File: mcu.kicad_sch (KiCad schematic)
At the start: 1 part, among them U1 MIMXRT1052CVJ5B

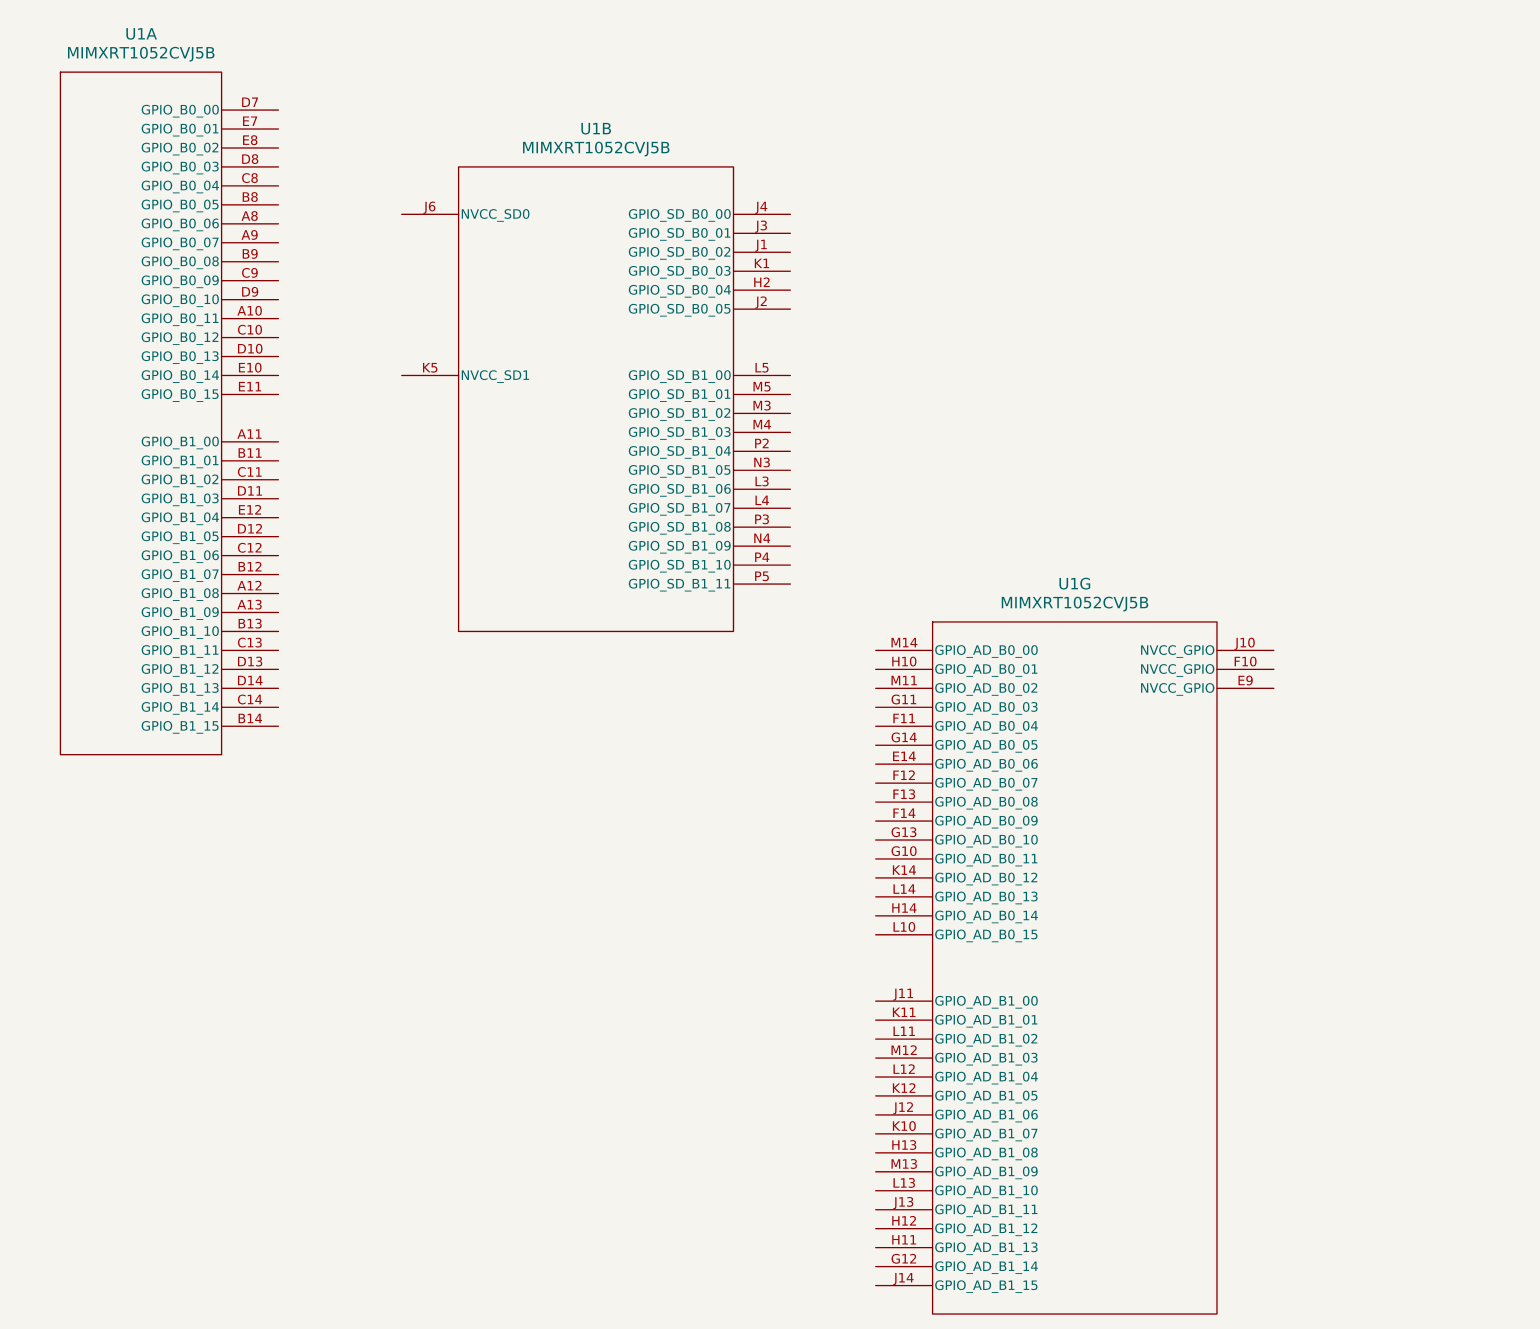
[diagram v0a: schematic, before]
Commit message: assign pin functions and started spe
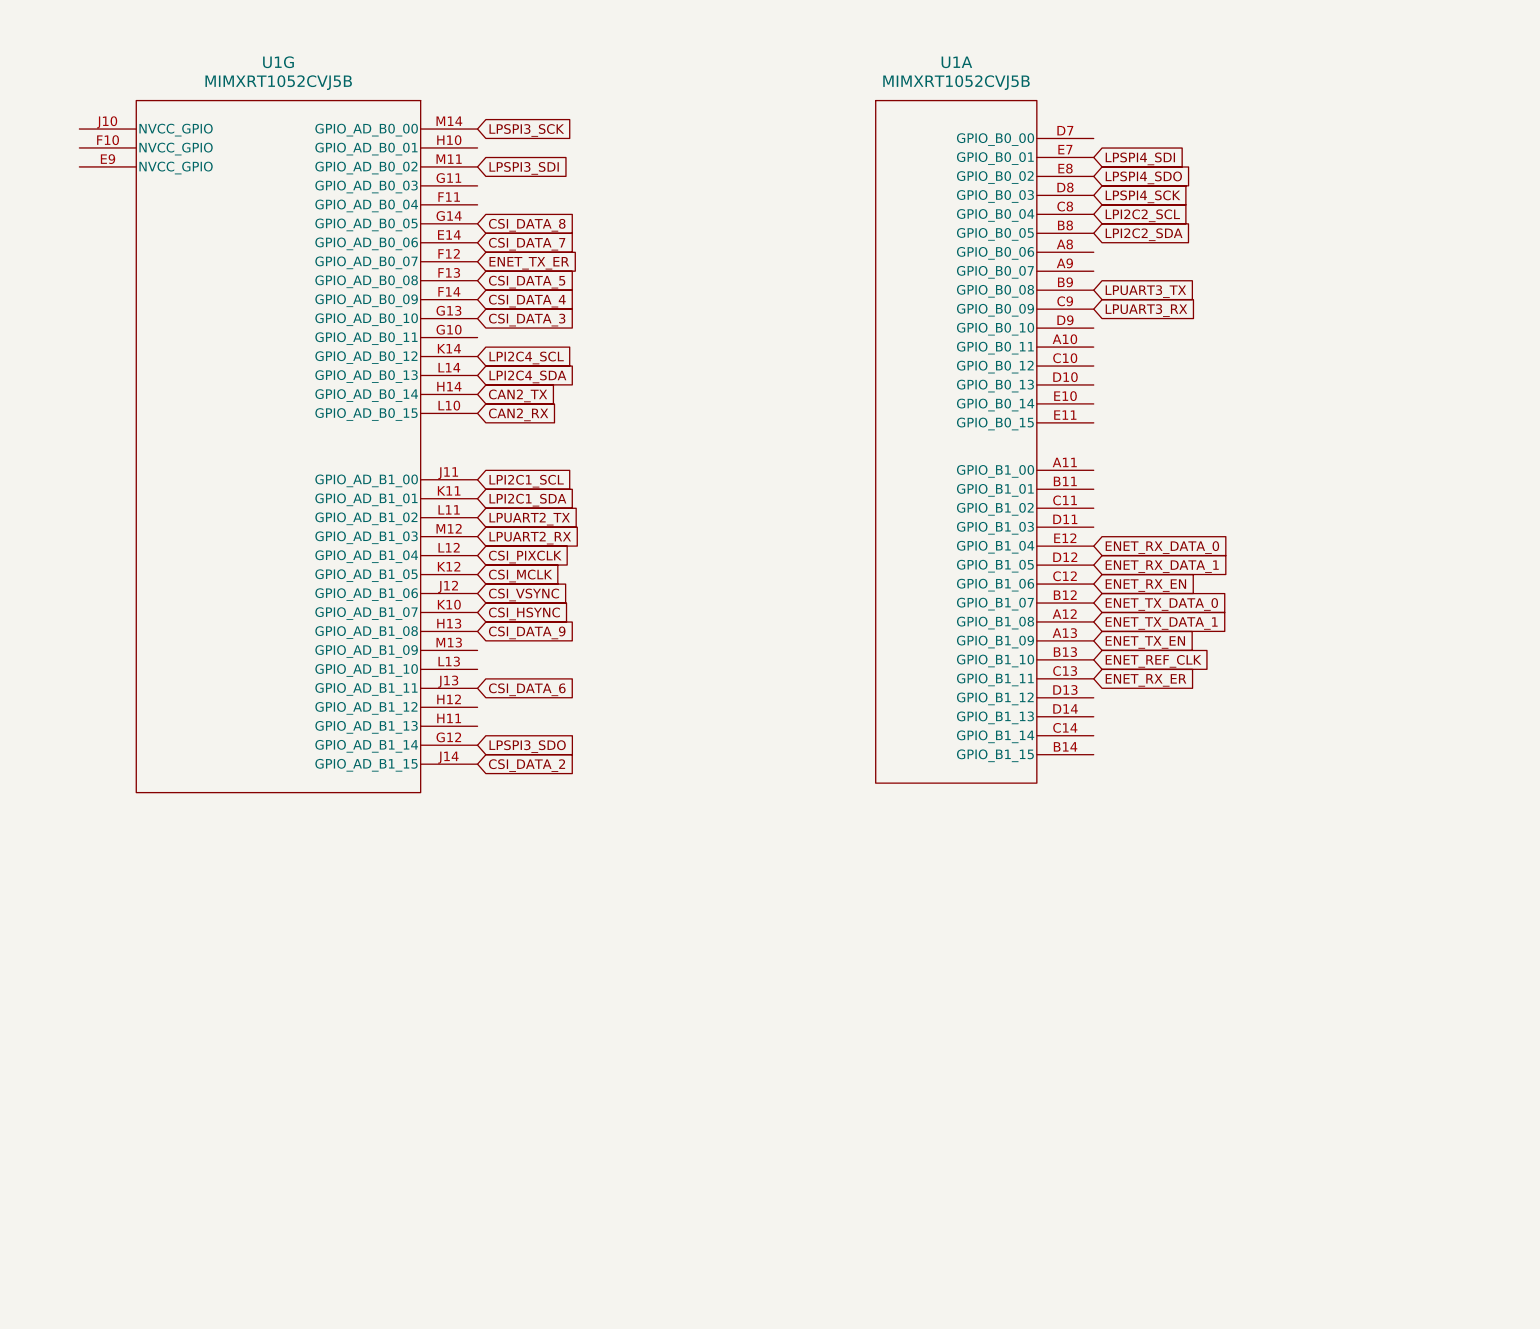
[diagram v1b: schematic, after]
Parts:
- removed unit 2 of U1
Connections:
- net CSI_DATA_7: now reaches U1.E14 (GPIO_AD_B0_06)
- net ENET_TX_ER: now reaches U1.F12 (GPIO_AD_B0_07)
- net CSI_DATA_5: now reaches U1.F13 (GPIO_AD_B0_08)
- net CSI_DATA_4: now reaches U1.F14 (GPIO_AD_B0_09)
- net LPSPI3_SDO: now reaches U1.G12 (GPIO_AD_B1_14)
- net CSI_DATA_3: now reaches U1.G13 (GPIO_AD_B0_10)
- net CSI_DATA_8: now reaches U1.G14 (GPIO_AD_B0_05)
- net CSI_DATA_9: now reaches U1.H13 (GPIO_AD_B1_08)
- net CAN2_TX: now reaches U1.H14 (GPIO_AD_B0_14)
- net LPI2C1_SCL: now reaches U1.J11 (GPIO_AD_B1_00)
- net CSI_VSYNC: now reaches U1.J12 (GPIO_AD_B1_06)
- net CSI_DATA_6: now reaches U1.J13 (GPIO_AD_B1_11)
- net CSI_DATA_2: now reaches U1.J14 (GPIO_AD_B1_15)
- net CSI_HSYNC: now reaches U1.K10 (GPIO_AD_B1_07)
- net LPI2C1_SDA: now reaches U1.K11 (GPIO_AD_B1_01)
- net CSI_MCLK: now reaches U1.K12 (GPIO_AD_B1_05)
- net LPI2C4_SCL: now reaches U1.K14 (GPIO_AD_B0_12)
- net CAN2_RX: now reaches U1.L10 (GPIO_AD_B0_15)
- net LPUART2_TX: now reaches U1.L11 (GPIO_AD_B1_02)
- net CSI_PIXCLK: now reaches U1.L12 (GPIO_AD_B1_04)
- net LPI2C4_SDA: now reaches U1.L14 (GPIO_AD_B0_13)
- net LPSPI3_SDI: now reaches U1.M11 (GPIO_AD_B0_02)
- net LPUART2_RX: now reaches U1.M12 (GPIO_AD_B1_03)
- net LPSPI3_SCK: now reaches U1.M14 (GPIO_AD_B0_00)
- net ENET_TX_DATA_1: now reaches U1.A12 (GPIO_B1_08)
- net ENET_TX_EN: now reaches U1.A13 (GPIO_B1_09)
- net ENET_TX_DATA_0: now reaches U1.B12 (GPIO_B1_07)
- net ENET_REF_CLK: now reaches U1.B13 (GPIO_B1_10)
- net LPI2C2_SDA: now reaches U1.B8 (GPIO_B0_05)
- net LPUART3_TX: now reaches U1.B9 (GPIO_B0_08)
- net ENET_RX_EN: now reaches U1.C12 (GPIO_B1_06)
- net ENET_RX_ER: now reaches U1.C13 (GPIO_B1_11)
- net LPI2C2_SCL: now reaches U1.C8 (GPIO_B0_04)
- net LPUART3_RX: now reaches U1.C9 (GPIO_B0_09)
- net ENET_RX_DATA_1: now reaches U1.D12 (GPIO_B1_05)
- net LPSPI4_SCK: now reaches U1.D8 (GPIO_B0_03)
- net ENET_RX_DATA_0: now reaches U1.E12 (GPIO_B1_04)
- net LPSPI4_SDI: now reaches U1.E7 (GPIO_B0_01)
- net LPSPI4_SDO: now reaches U1.E8 (GPIO_B0_02)
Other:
- moved on the sheet: U1A, U1G

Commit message: finished v1
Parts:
- added C58: 4.7uF, symbol Device:C_Small
- added C59, C60, C61: 100nF, symbol Device:C_Small
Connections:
- net +3.3V: now reaches U1.E9 (NVCC_GPIO)
- net +3.3V: now also U1.F10 (NVCC_GPIO), U1.J10 (NVCC_GPIO), C58.1, C59.1, C60.1, C61.1
- net DIO4: now reaches U1.F11 (GPIO_AD_B0_04)
- net DIO0: now reaches U1.G10 (GPIO_AD_B0_11)
- net HOPERF_RST: now reaches U1.G11 (GPIO_AD_B0_03)
- net LPSPI3_CS: now reaches U1.H10 (GPIO_AD_B0_01)
- net ADC2_2: now reaches U1.H11 (GPIO_AD_B1_13)
- net ADC2_1: now reaches U1.H12 (GPIO_AD_B1_12)
- net ADC2_15: now reaches U1.L13 (GPIO_AD_B1_10)
- net ADC2_14: now reaches U1.M13 (GPIO_AD_B1_09)
- net STB: now reaches U1.A10 (GPIO_B0_11)
- net PWM1_A_3: now reaches U1.A11 (GPIO_B1_00)
- net INT_N_IO_EXP: now reaches U1.A8 (GPIO_B0_06)
- net RESET_N_IO_EXP: now reaches U1.A9 (GPIO_B0_07)
- net PWM1_B_3: now reaches U1.B11 (GPIO_B1_01)
- net RESET_N: now reaches U1.B14 (GPIO_B1_15)
- net LDO_EN: now reaches U1.C10 (GPIO_B0_12)
- net PWM2_A_3: now reaches U1.C11 (GPIO_B1_02)
- net INT_N: now reaches U1.C14 (GPIO_B1_14)
- net PWDN: now reaches U1.D10 (GPIO_B0_13)
- net PWM2_B_3: now reaches U1.D11 (GPIO_B1_03)
- net INH: now reaches U1.D13 (GPIO_B1_12)
- net WAKE: now reaches U1.D14 (GPIO_B1_13)
- net LPSPI4_CS: now reaches U1.D7 (GPIO_B0_00)
- net SHDN: now reaches U1.D9 (GPIO_B0_10)
- net XRS: now reaches U1.E10 (GPIO_B0_14)
- new net GND: C58.2, C59.2, C60.2, C61.2
- no-connect marks 0 -> 1
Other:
- company: (none) -> Northeastern University
- title: (none) -> RT1050 DevBoard for Project Horizon
- moved on the sheet: U1A, U1G

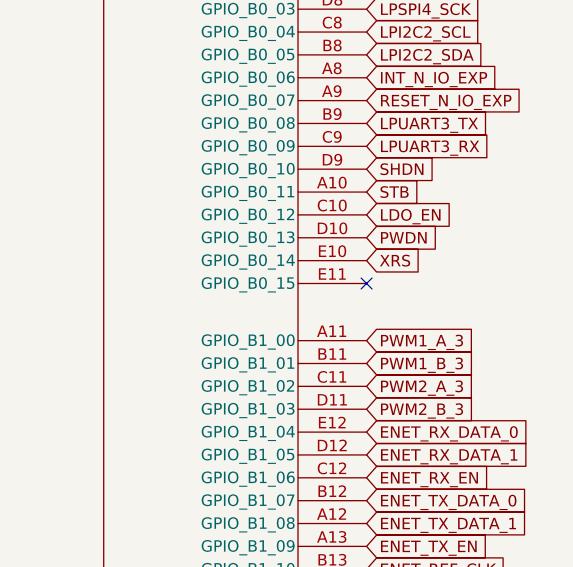
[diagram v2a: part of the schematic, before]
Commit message: added load switches
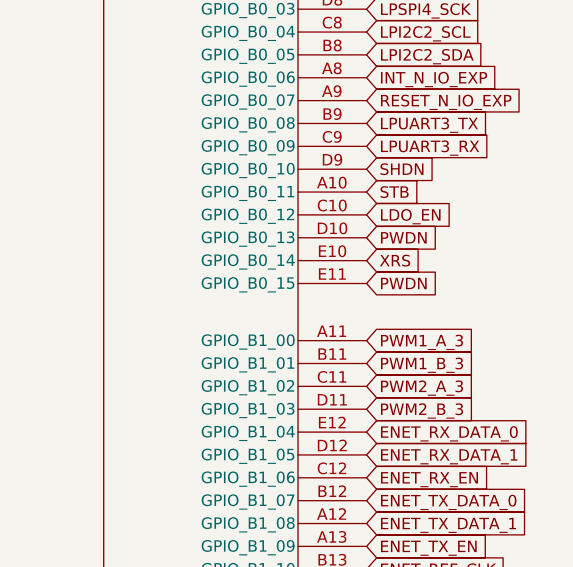
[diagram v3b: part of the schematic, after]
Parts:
- C58, C59, C60, C61: footprint (none) -> Capacitor_SMD:C_0402_1005Metric
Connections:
- net PWDN: now also U1.E11 (GPIO_B0_15)
- no-connect marks 1 -> 0
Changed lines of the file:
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@@
 		(color 0 0 0 0)
-	)
-	(no_connect
-		(at 196.85 68.58)
 	)
 	(wire
@@
 		(property "Intersheetrefs" "${INTERSHEET_REFS}"
 			(at 210.9628 43.18 0)
+			(effects
+				(font
+					(size 1.27 1.27)
+				)
+				(justify left)
+				(hide yes)
+			)
+		)
+	)
+	(global_label "PWDN"
+		(shape input)
+		(at 196.85 68.58 0)
+		(fields_autoplaced yes)
+		(effects
+			(font
+				(size 1.27 1.27)
+			)
+			(justify left)
+		)
+		(property "Intersheetrefs" "${INTERSHEET_REFS}"
+			(at 205.1571 68.58 0)
 			(effects
 				(font
@@
 			)
 		)
-		(property "Footprint" ""
+		(property "Footprint" "Capacitor_SMD:C_0402_1005Metric"
 			(at 19.05 25.4 0)
 			(effects
@@
 			)
 		)
-		(property "Footprint" ""
+		(property "Footprint" "Capacitor_SMD:C_0402_1005Metric"
 			(at 39.37 25.4 0)
 			(effects
@@
 			)
 		)
-		(property "Footprint" ""
+		(property "Footprint" "Capacitor_SMD:C_0402_1005Metric"
 			(at 49.53 25.4 0)
 			(effects
@@
 			)
 		)
-		(property "Footprint" ""
+		(property "Footprint" "Capacitor_SMD:C_0402_1005Metric"
 			(at 29.21 25.4 0)
 			(effects

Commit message: save before sdram redesign
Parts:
- C58, C59, C60, C61: footprint Capacitor_SMD:C_0402_1005Metric -> Capacitor_SMD:C_0201_0603Metric
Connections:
- net INT_N_IO_EXP is gone; now on net DIO4: U1.A8 (GPIO_B0_06)
- net RESET_N_IO_EXP is gone; now on net DIO0: U1.A9 (GPIO_B0_07)
- net DIO0: no longer U1.G10 (GPIO_AD_B0_11)
- net DIO4: no longer U1.F11 (GPIO_AD_B0_04)
- net LDO_EN: no longer names the net of U1.C10 (GPIO_B0_12)
- net PWDN: no longer names the net of U1.E11 (GPIO_B0_15)
- net PWDN: no longer U1.D10 (GPIO_B0_13)
- net XRS: no longer names the net of U1.E10 (GPIO_B0_14)
- new net GPIO_AD_B0_04: U1.F11 (GPIO_AD_B0_04)
- new net GPIO_B0_13: U1.D10 (GPIO_B0_13)
- no-connect marks 0 -> 4

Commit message: SDRAM redo and finished boards
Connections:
- net SHDN: no longer names the net of U1.D9 (GPIO_B0_10)
- no-connect marks 4 -> 5
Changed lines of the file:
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@@
+	)
+	(no_connect
+		(at 196.85 55.88)
 	)
 	(no_connect
@@
 				(hide yes)
 			)
-		)
-	)
-	(global_label "SHDN"
-		(shape input)
-		(at 196.85 55.88 0)
-		(effects
-			(font
-				(size 1.27 1.27)
-			)
-			(justify left)
-		)
-		(property "Intersheetrefs" "${INTERSHEET_REFS}"
-			(at 196.85 55.88 0)
-			(effects
-				(font
-					(size 1.27 1.27)
-				)
-				(hide yes)
-			)
